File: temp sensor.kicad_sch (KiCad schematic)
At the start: 52 parts, among them IC1 ESP32-C3-MINI-1, J1 USB_C_Receptacle_USB2.0, J2 Conn_01x02_Male, J3 Conn_01x06_Male, J4 USB_B_Micro, J5 Conn_01x02_Male, J6 Conn_01x02_Male, Q1 BC847BDW1, SW1 SW_Push_Right_Angle, SW2 SW_Push_Right_Angle, U1 SHTC3, U2 TLV62569DBV, U3 BME280, U4 Si7020-A20, U5 SN65220

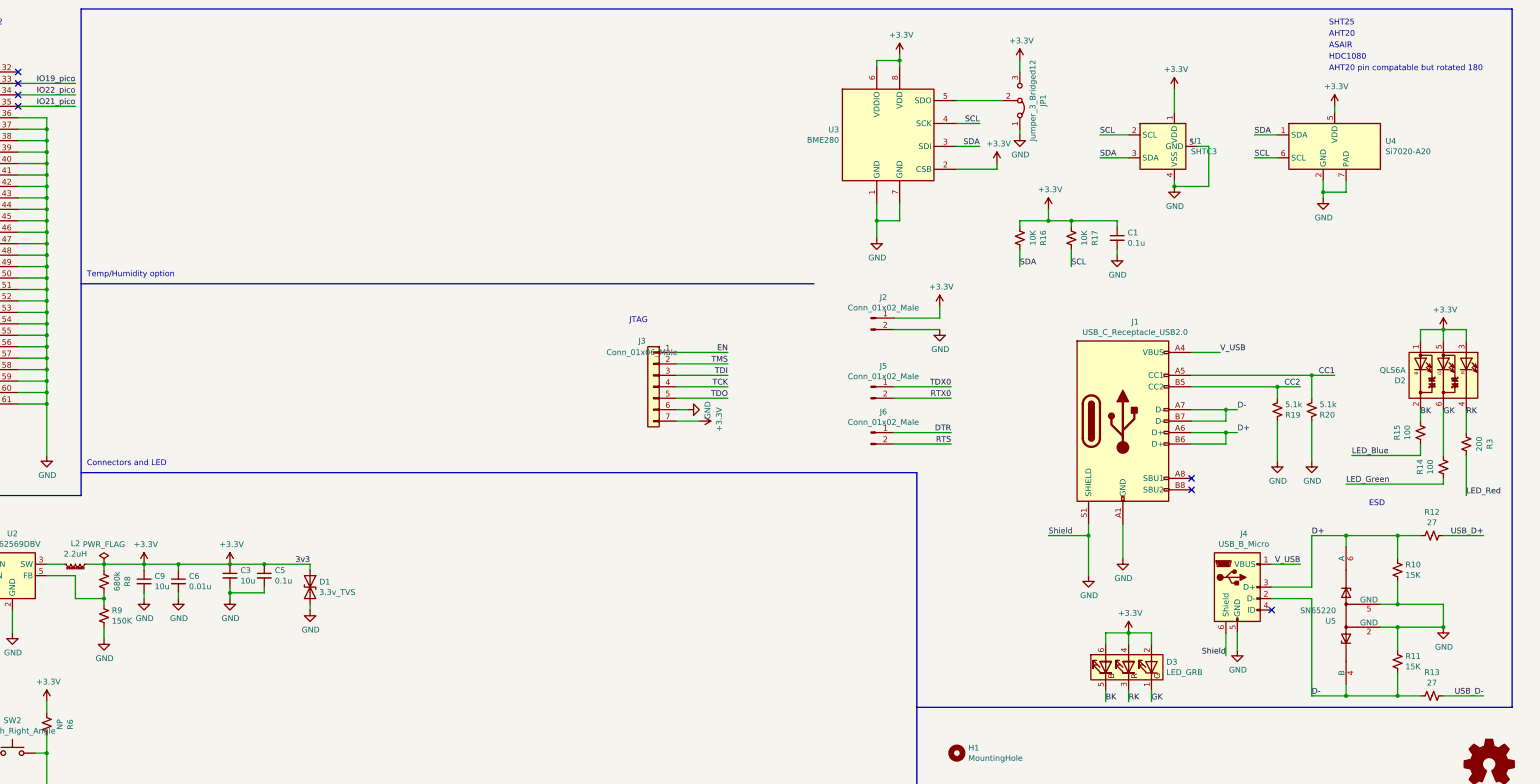
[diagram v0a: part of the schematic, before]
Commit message: added support for AS7341 and removed support for one of the temp/humidity sensors
Signed-off-by: lokimetasmith <lokimail@gmail.com>
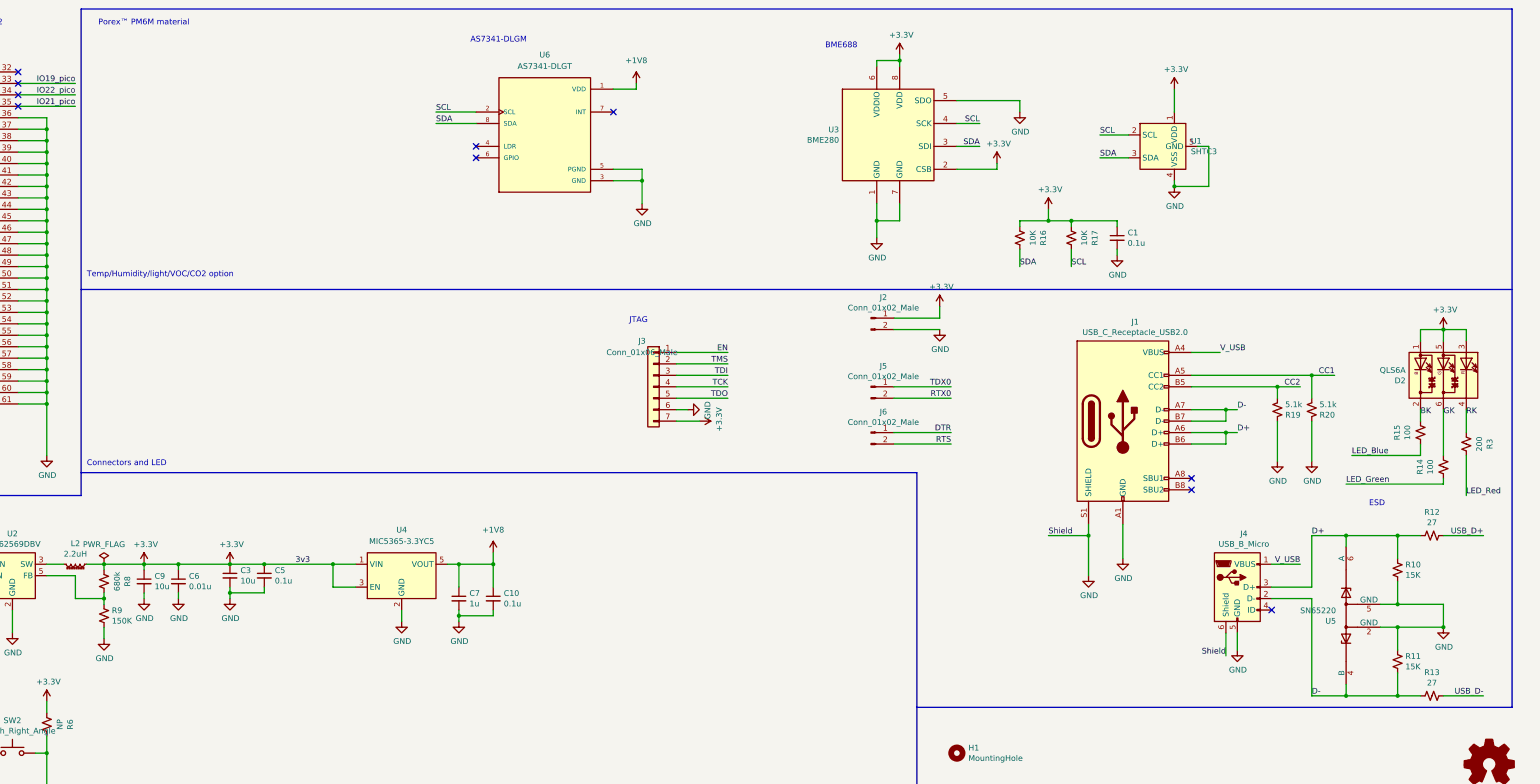
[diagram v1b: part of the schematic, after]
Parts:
- removed D1: 3.3v_TVS, Diode_SMD:D_SOD-323_HandSoldering, symbol temp-sensor-rescue:D_TVS-Device-temp-sensor-rescue
- removed D3: LED_GRB, Twig:99-235-RSGBB7C-A22-2D, symbol twig:LED_GRB
- removed JP1: Jumper_3_Bridged12, Twig:Jumper_0603_1608Metric, symbol Jumper:Jumper_3_Bridged12
- removed U4: Si7020-A20, Package_DFN_QFN:DFN-6-1EP_3x3mm_P1mm_EP1.5x2.4mm, symbol temp-sensor-rescue:Si7020-A20-Sensor_Humidity-temp-sensor-rescue
- added C10: 0.1u, Capacitor_SMD:C_0603_1608Metric, symbol temp-sensor-rescue:C_Small-Device-temp-sensor-rescue
- added C7: 1u, Capacitor_SMD:C_0402_1005Metric, symbol temp-sensor-rescue:C_Small-Device-temp-sensor-rescue
- added U4: MIC5365-3.3YC5, Package_TO_SOT_SMD:SOT-353_SC-70-5, symbol Regulator_Linear:MIC5365-3.3YC5
- added U6: AS7341-DLGT, Twig:PSON80P310X200X110-8N, symbol AS7341-DLGT:AS7341-DLGT
- R1, R10, R11, R12, R13, R14, R15, R16, R17, R19, R2, R20, R21, R3, R4, R5, R6, R7, R8, R9: footprint Resistor_SMD:R_0603_1608Metric -> Resistor_SMD:R_0402_1005Metric
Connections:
- net +3V3: now also U4.1 (VIN), U4.3 (EN)
- net GND: now also U3.5 (SDO), C10.2, C7.2, U4.2 (GND), U6.3 (GND), U6.5 (PGND)
- net I38_pico: now also U6.8 (SDA)
- net IO13_pico: now also U6.2 (SCL)
- new net +1V8: C10.1, C7.1, U4.5 (VOUT), U6.1 (VDD)
- no-connect marks 21 -> 24
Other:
- note added: "AS7341-DLGM"
- note added: "BME688"
- note added: "Porex™ PM6M material"
- note added: "Temp/Humidity/light/VOC/CO2 option"
- note removed: "AHT20"
- note removed: "AHT20 pin compatable but rotated 180"
- note removed: "ASAIR"
- note removed: "HDC1080"
- note removed: "SHT25"
- note removed: "Temp/Humidity option"

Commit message: added cutout model, minor changes to pcb
Signed-off-by: lokimetasmith <lokimail@gmail.com>
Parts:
- added SYM1: SYM_Arrow_Normal, Twig:Sensor Keepout block, symbol Graphic:SYM_Arrow_Normal
- C1, C10, C2, C4, C5: footprint Capacitor_SMD:C_0603_1608Metric -> Capacitor_SMD:C_0402_1005Metric; Configuration (none) -> all; Digikey Part Number (none) -> 1276-1001-1-ND; Manufacturer_Part_Number EMK107B7104KAHT -> EMK105B7104KVHF; Mouser Part Number 963-EMK107B7104KAHT -> 963-EMK105B7104KVHF; PARTREV (none) -> V3
- C3, C8, C9, D2, IC1, J1, J2, J3, J4, J5, J6, L2, LOGO1, Q1, SW1, SW2, U2, U5: Configuration (none) -> all
- C6: footprint Capacitor_SMD:C_0603_1608Metric -> Capacitor_SMD:C_0402_1005Metric; Configuration (none) -> all; Manufacturer_Part_Number EMK107B7104KAHT -> EMK105B7103KVHF; Mouser Part Number 963-EMK107B7104KAHT -> 963-EMK105B7103KVHF; PARTREV (none) -> V3
- C7: footprint Capacitor_SMD:C_0402_1005Metric -> Capacitor_SMD:C_0603_1608Metric; Configuration (none) -> all; Manufacturer_Name (none) -> Taiyo Yuden; Manufacturer_Part_Number (none) -> EMK107B7105KA-T; Mouser Part Number (none) -> 963-EMK107B7105KA-T; Mouser Price/Stock (none) -> $0.10/110000
- H1, H2, H3, R10, R11, R12, R13, R14, R15, R16, R17, R19, R20, R21, R4, R5, R6, R7, R8, R9: Configuration (none) -> all; PARTREV (none) -> V3
- R1, R2: Alternate Part Number 1 (none) -> RC0402FR-07499RL; Configuration (none) -> all; Digikey Part Number (none) -> 311-499LRCT-ND; PARTREV (none) -> V3
- R3: Alternate Part Number 1 (none) -> PFR05S-201-FNH; Configuration (none) -> all; Digikey Part Number (none) -> 2037-PFR05S-201-FNHCT-ND; PARTREV (none) -> V3
- U1: Configuration (none) -> 1,2
- U3: Configuration (none) -> 2-BMP280,3-BME280,4-BME688
- U4: Configuration (none) -> 4
- U6: Configuration (none) -> 4; STANDARD IPC7351B -> (none)
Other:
- note added: "1: SHTC3 Temp/Humidty"
- note added: "2: BMP280 Temp/Pressure, SHTC3 Temp/Humidity"
- note added: "3: BME280 temp/humidity/pressure"
- note added: "4: BMP688 Temp/Humidity/Pressure/VOC, Light"
- note added: "Configuration"
- note added: "Located near processor"
- note added: "Mounting holes are used for assembly as well as injection molding alignment"
- note added: "Porex PM6M material, or teflon plumbing tape"
- note removed: "Porex™ PM6M material"
- note removed: "need to add color sensor and voc"

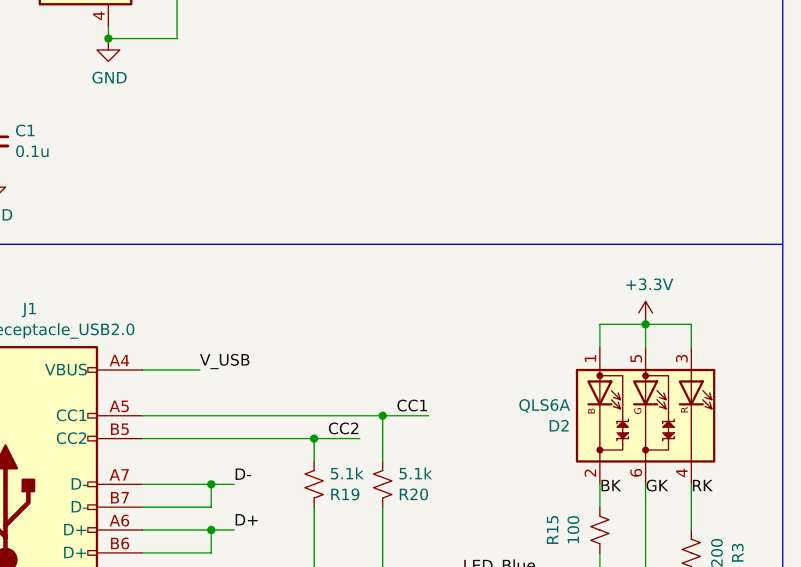
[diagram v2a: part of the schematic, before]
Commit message: added led cutout block
Signed-off-by: lokimetasmith <lokimail@gmail.com>
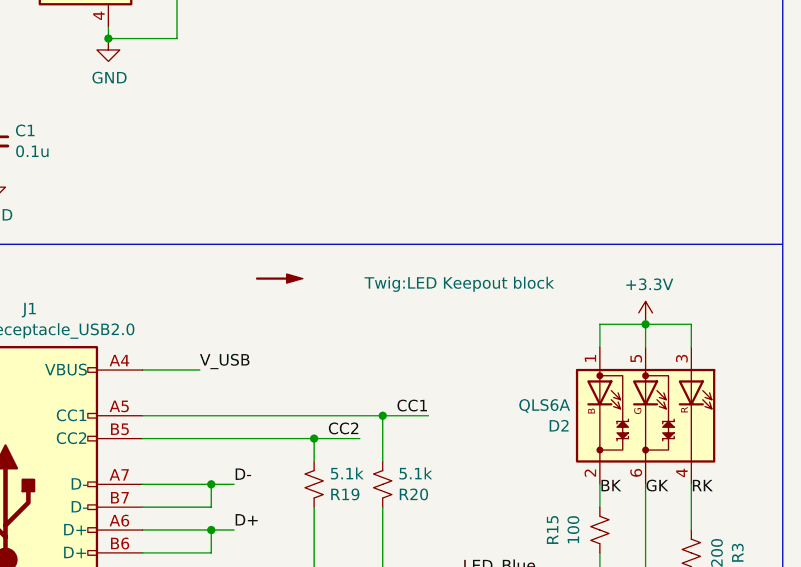
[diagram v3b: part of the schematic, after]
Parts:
- added SYM2: SYM_Arrow_Normal, Twig:LED Keepout block, symbol Graphic:SYM_Arrow_Normal
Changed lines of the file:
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@@
     (pin "2")
+  )
+  (symbol (lib_id "Graphic:SYM_Arrow_Normal") (at 363.22 78.74 0) (unit 1)
+    (in_bom yes) (on_board yes)
+    (property "Reference" "SYM2" (id 0) (at 363.22 77.216 0)
+      (effects (font (size 1.27 1.27)) hide)
+    )
+    (property "Value" "SYM_Arrow_Normal" (id 1) (at 363.474 80.01 0)
+      (effects (font (size 1.27 1.27)) hide)
+    )
+    (property "Footprint" "Twig:LED Keepout block" (id 2) (at 393.7 80.01 0)
+      (effects (font (size 1.27 1.27)) (justify right bottom))
+    )
+    (property "Datasheet" "~" (id 3) (at 363.22 78.74 0)
+      (effects (font (size 1.27 1.27)) hide)
+    )
   )
   (symbol (lib_id "Graphic:SYM_Arrow_Normal") (at 105.41 68.58 0) (unit 1)
@@
       (reference "SYM1") (unit 1) (value "SYM_Arrow_Normal") (footprint "Twig:Sensor Keepout block")
     )
+    (path "/4a8586ae-174b-41e6-93c1-296c6bd66835"
+      (reference "SYM2") (unit 1) (value "SYM_Arrow_Normal") (footprint "Twig:LED Keepout block")
+    )
     (path "/00000000-0000-0000-0000-000060a2e91b"

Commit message: cribbed schematic corrections from https://github.com/esp-rs/esp-rust-board/tree/master/hardware/esp-rust-board
tweaked part layout, added back in zener 3v3 diode, added filter diode, and made minor tweaks.

Signed-off-by: lokimetasmith <lokimail@gmail.com>
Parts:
- added C11: 6.8p, Capacitor_SMD:C_0402_1005Metric, symbol temp-sensor-rescue:C_Small-Device-temp-sensor-rescue
- added D1: 3.3v_TVS, Diode_SMD:D_SOD-323, symbol temp-sensor-rescue:D_TVS-Device-temp-sensor-rescue
- D2: footprint LED_SMD:LED_Cree-PLCC6_4.7x1.5mm -> Twig:LED_Cree-PLCC6_4.7x1.5mm
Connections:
- net +3V3: now also C11.1, D1.1 (A1)
- net GND: now also D1.2 (A2)
- net at R8.1, R9.2, U2.5 (FB): now also C11.2
- no-connect marks 24 -> 23
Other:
- moved on the sheet: C10, C3, C5, C6, C7, C9, R8, R9, U4
